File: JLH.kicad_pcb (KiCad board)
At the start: 2 copper layers, 170 x 200 mm, 51 parts, among them J1 Вход, J2 Выход, J3 B2P-VH, Q1 КТ361Г, Q2 КТ801А, Q3 2Т803А, Q4 2Т803А, Q5 КТ361Г, Q6 КТ801А, Q7 2Т803А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

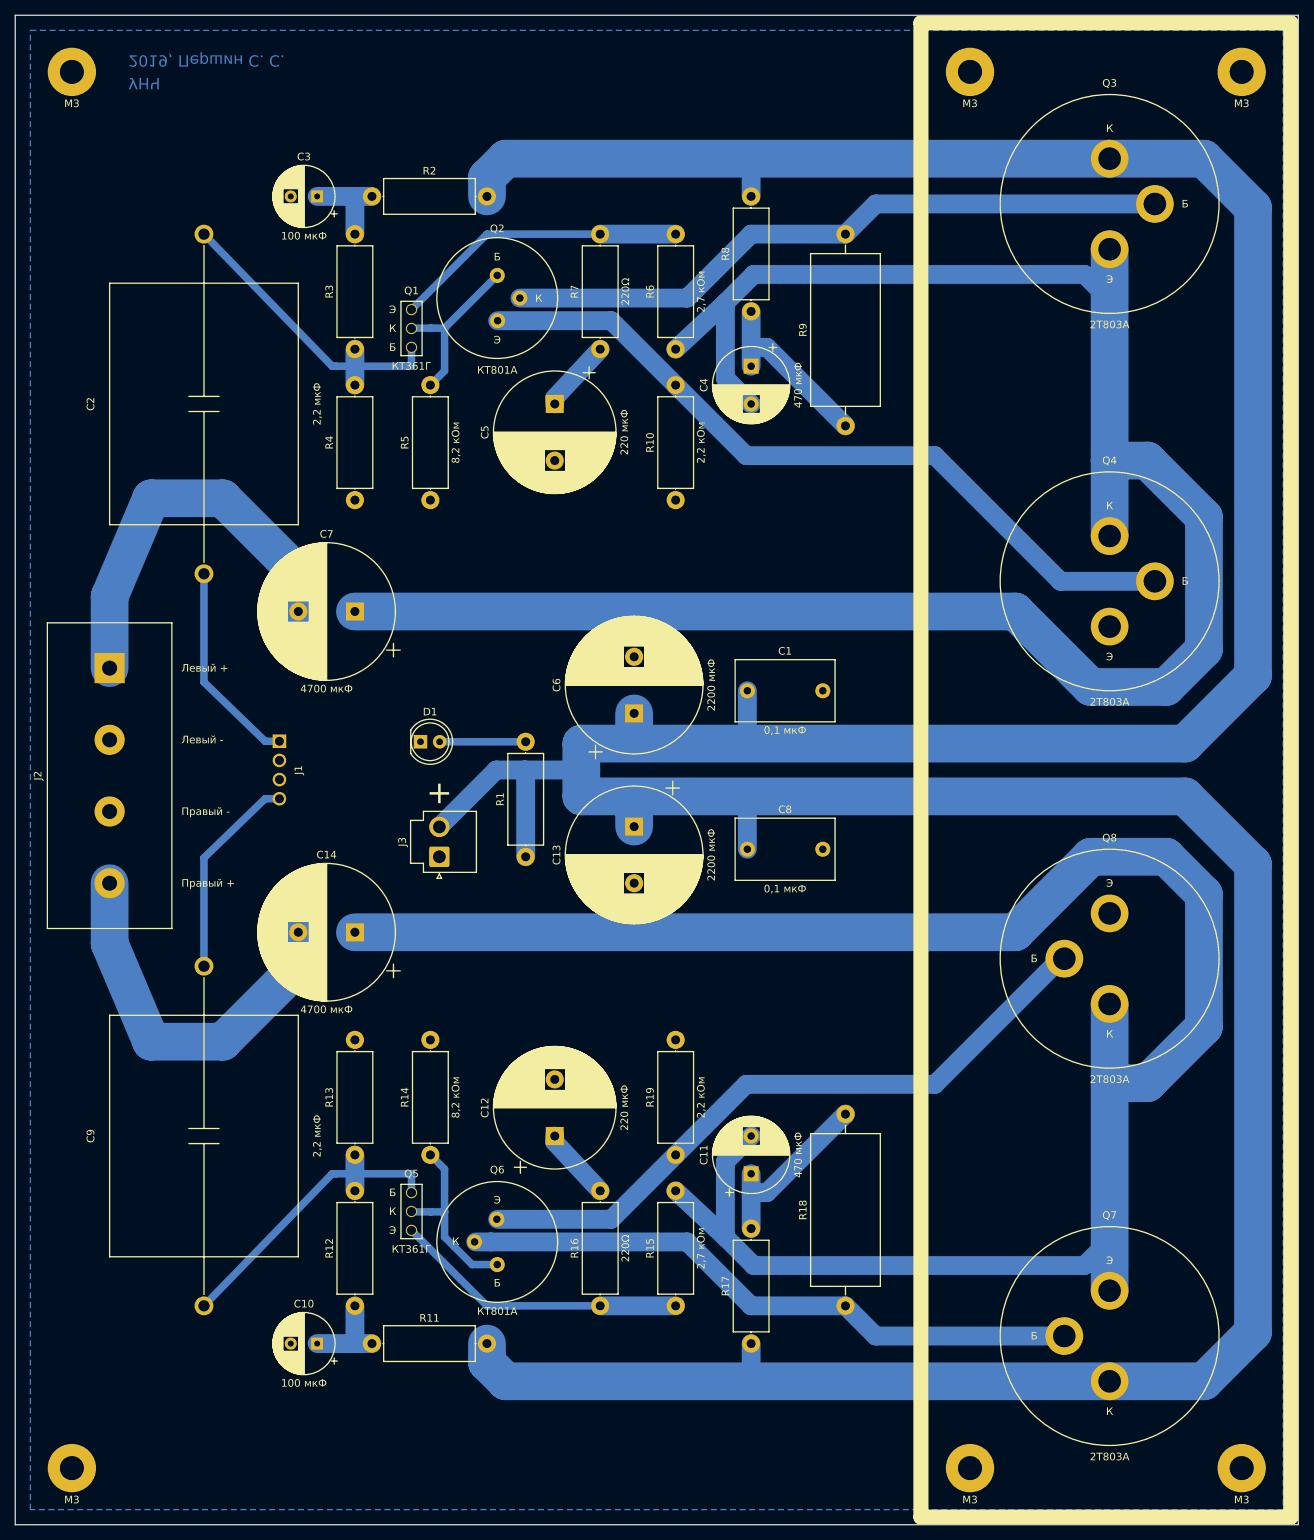
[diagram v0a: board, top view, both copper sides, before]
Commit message: Fixed GND
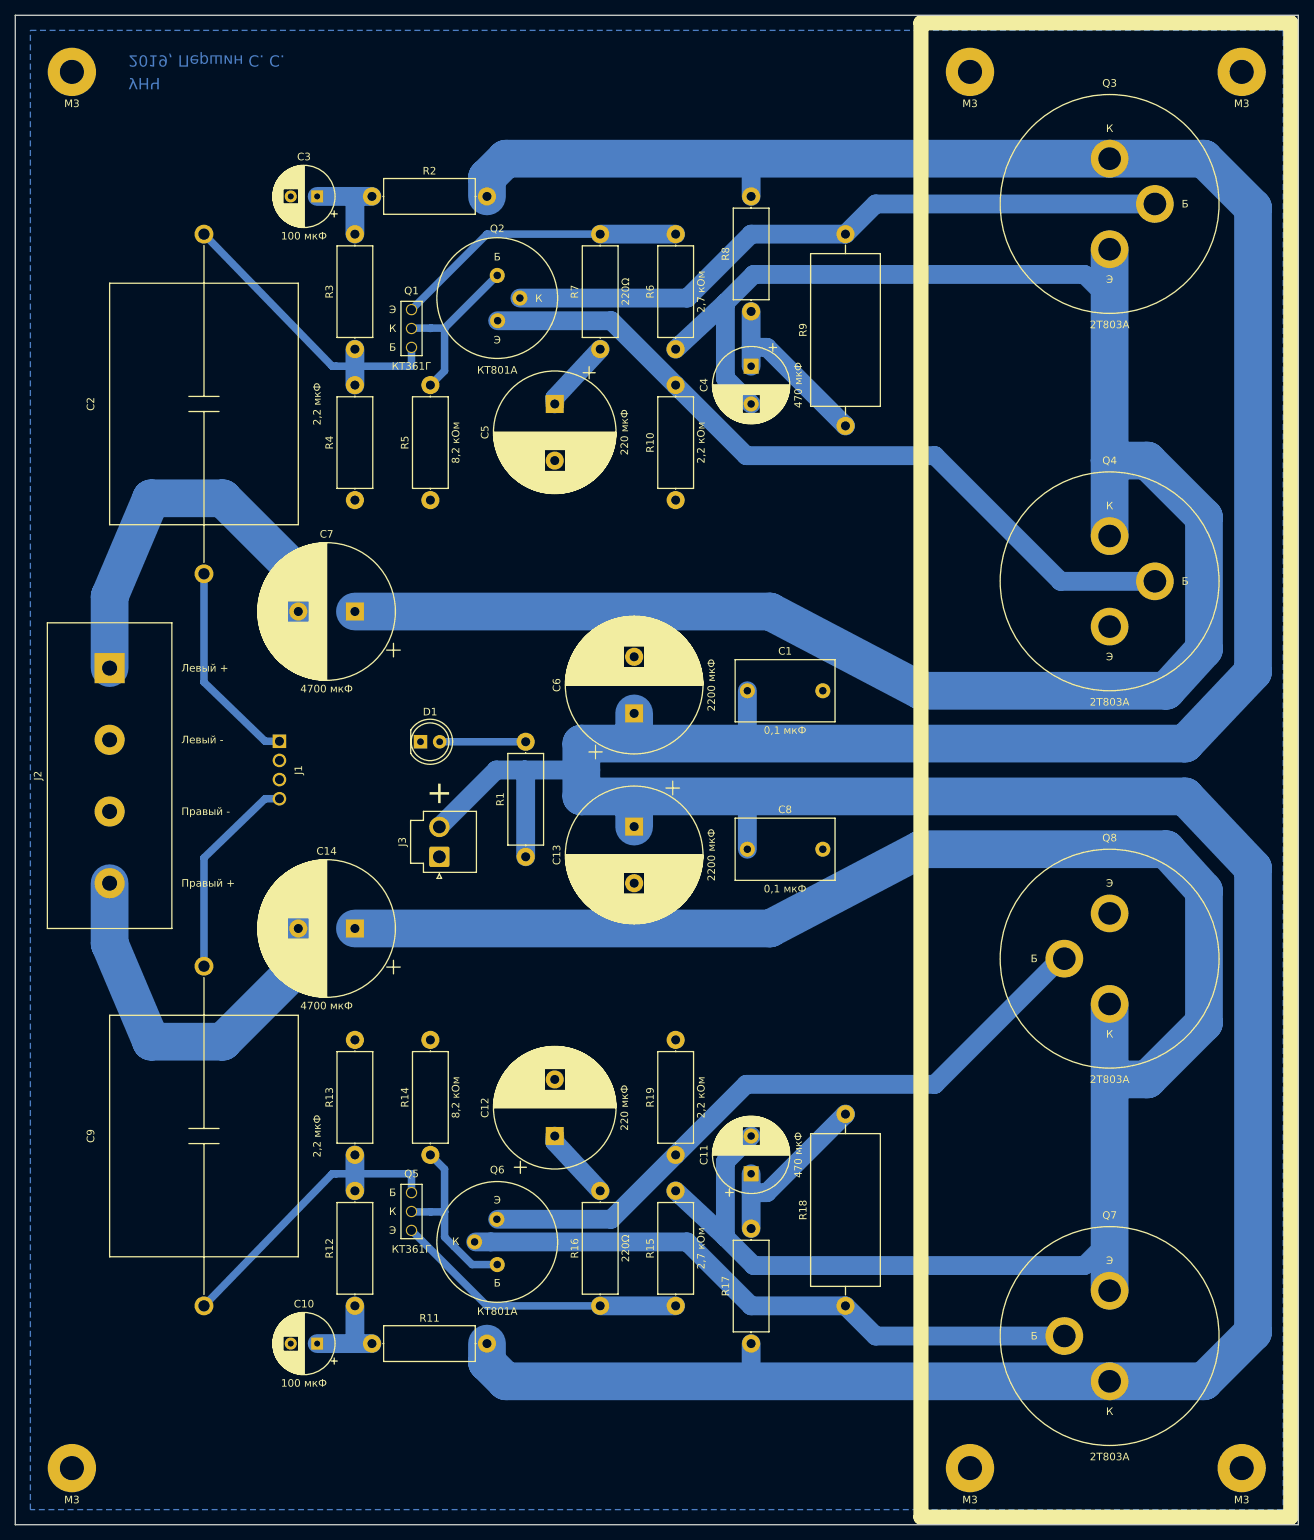
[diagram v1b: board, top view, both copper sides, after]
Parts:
- moved C14 0.50 mm to (65.0, 147.0)
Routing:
- net Net-(C4-Pad2): track 265.8 -> 264.6 mm
- net Net-(C11-Pad2): track 265.8 -> 264.6 mm
- net /Правый канал/OUT+: track 50.3 -> 50.8 mm
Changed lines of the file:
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@@
     (solder_mask_min_width 0.25)
     (aux_axis_origin 0 0)
-    (visible_elements 7FFFFFFF)
+    (visible_elements 7FFFEFFF)
     (pcbplotparams
       (layerselection 0x010fc_ffffffff)
@@
   )
   (module Capacitor_THT:CP_Radial_D18.0mm_P7.50mm (layer F.Cu)
-    (at 65 147.5 180)
+    (at 65 147 180)
     (descr "CP, Radial series, Radial, pin pitch=7.50mm, , diameter=18mm, Electrolytic Capacitor")
     (tags "CP Radial series Radial pin pitch 7.50mm  diameter 18mm Electrolytic Capacitor")
@@
   (segment (start 177.5 45) (end 165 45) (width 5) (layer B.Cu) (net 8))
   (segment (start 184 51.5) (end 177.5 45) (width 5) (layer B.Cu) (net 8))
-  (segment (start 184 113.5) (end 184 51.5) (width 5) (layer B.Cu) (net 8))
-  (segment (start 175 122.5) (end 184 113.5) (width 5) (layer B.Cu) (net 8))
+  (segment (start 184 113) (end 184 51.5) (width 5) (layer B.Cu) (net 8))
+  (segment (start 175 122.5) (end 184 113) (width 5) (layer B.Cu) (net 8))
   (segment (start 95 126) (end 95 122.5) (width 5) (layer B.Cu) (net 8))
   (segment (start 95 122.5) (end 175 122.5) (width 5) (layer B.Cu) (net 8))
@@
   (segment (start 95 129.5) (end 95 126) (width 5) (layer B.Cu) (net 8))
   (segment (start 175 129.5) (end 95 129.5) (width 5) (layer B.Cu) (net 8))
-  (segment (start 184 138.5) (end 175 129.5) (width 5) (layer B.Cu) (net 8))
-  (segment (start 184 200.5) (end 184 138.5) (width 5) (layer B.Cu) (net 8))
+  (segment (start 184 139) (end 175 129.5) (width 5) (layer B.Cu) (net 8))
+  (segment (start 184 200.5) (end 184 139) (width 5) (layer B.Cu) (net 8))
   (segment (start 177.5 207) (end 184 200.5) (width 5) (layer B.Cu) (net 8))
   (segment (start 53.1 122.19) (end 55 122.19) (width 1) (layer B.Cu) (net 9) (status 20))
@@
   (segment (start 165 57) (end 165 85) (width 5) (layer B.Cu) (net 11))
   (segment (start 165 85) (end 165 95) (width 5) (layer B.Cu) (net 11))
-  (segment (start 177.5 92.5) (end 170 85) (width 5) (layer B.Cu) (net 11))
-  (segment (start 152.5 105) (end 162.5 115) (width 5) (layer B.Cu) (net 11))
-  (segment (start 65 105) (end 152.5 105) (width 5) (layer B.Cu) (net 11))
-  (segment (start 162.5 115) (end 172.5 115) (width 5) (layer B.Cu) (net 11))
-  (segment (start 172.5 115) (end 177.5 110) (width 5) (layer B.Cu) (net 11))
-  (segment (start 170 85) (end 165 85) (width 5) (layer B.Cu) (net 11))
-  (segment (start 177.5 110) (end 177.5 92.5) (width 5) (layer B.Cu) (net 11))
+  (segment (start 120 105) (end 65 105) (width 5) (layer B.Cu) (net 11))
+  (segment (start 165 85) (end 170 85) (width 5) (layer B.Cu) (net 11))
+  (segment (start 170 85) (end 177.5 92.5) (width 5) (layer B.Cu) (net 11))
+  (segment (start 177.5 92.5) (end 177.5 110) (width 5) (layer B.Cu) (net 11))
+  (segment (start 177.5 110) (end 172.5 115.5) (width 5) (layer B.Cu) (net 11))
+  (segment (start 172.5 115.5) (end 140 115.5) (width 5) (layer B.Cu) (net 11))
+  (segment (start 140 115.5) (end 120 105) (width 5) (layer B.Cu) (net 11))
   (segment (start 91.48 76.7) (end 97.5 70.24) (width 2.5) (layer B.Cu) (net 12) (status 30))
   (segment (start 91.48 77.5) (end 91.48 76.7) (width 2.5) (layer B.Cu) (net 12) (status 30))
@@
   (segment (start 38 162) (end 32.5 149) (width 5) (layer B.Cu) (net 15))
   (segment (start 47.5 162) (end 38 162) (width 5) (layer B.Cu) (net 15))
-  (segment (start 57.5 147.5) (end 57.5 152) (width 5) (layer B.Cu) (net 15))
+  (segment (start 57.5 147) (end 57.5 152) (width 5) (layer B.Cu) (net 15))
   (segment (start 57.5 152) (end 47.5 162) (width 5) (layer B.Cu) (net 15))
   (segment (start 62.5 179.5) (end 65 179.5) (width 1) (layer B.Cu) (net 16))
@@
   (segment (start 117.5 182) (end 119.6 182) (width 2.5) (layer B.Cu) (net 18))
   (segment (start 119.6 182) (end 130 171.6) (width 2.5) (layer B.Cu) (net 18) (status 20))
+  (segment (start 172.5 136.5) (end 140 136.5) (width 5) (layer B.Cu) (net 19))
+  (segment (start 140 136.5) (end 120 147) (width 5) (layer B.Cu) (net 19))
   (segment (start 161.66 191.66) (end 163.82 189.5) (width 2.5) (layer B.Cu) (net 19))
   (segment (start 114.09 187.91) (end 117.84 191.66) (width 2.5) (layer B.Cu) (net 19))
@@
   (segment (start 107.5 181.76) (end 114.09 187.91) (width 2.5) (layer B.Cu) (net 19) (status 10))
   (segment (start 165 157) (end 165 195) (width 5) (layer B.Cu) (net 19))
-  (segment (start 152.5 147.5) (end 162.5 137.5) (width 5) (layer B.Cu) (net 19))
-  (segment (start 170 167.5) (end 165 167.5) (width 5) (layer B.Cu) (net 19))
-  (segment (start 162.5 137.5) (end 172.5 137.5) (width 5) (layer B.Cu) (net 19))
-  (segment (start 177.5 160) (end 170 167.5) (width 5) (layer B.Cu) (net 19))
-  (segment (start 65 147.5) (end 152.5 147.5) (width 5) (layer B.Cu) (net 19))
-  (segment (start 172.5 137.5) (end 177.5 142.5) (width 5) (layer B.Cu) (net 19))
-  (segment (start 177.5 142.5) (end 177.5 160) (width 5) (layer B.Cu) (net 19))
+  (segment (start 170 167) (end 165 167) (width 5) (layer B.Cu) (net 19))
+  (segment (start 177.5 159.5) (end 170 167) (width 5) (layer B.Cu) (net 19))
+  (segment (start 65 147) (end 120 147) (width 5) (layer B.Cu) (net 19))
+  (segment (start 172.5 136.5) (end 177.5 142) (width 5) (layer B.Cu) (net 19))
+  (segment (start 177.5 142) (end 177.5 159.5) (width 5) (layer B.Cu) (net 19))
   (segment (start 91.48 175.3) (end 97.5 181.76) (width 2.5) (layer B.Cu) (net 20) (status 30))
   (segment (start 91.48 174.5) (end 91.48 175.3) (width 2.5) (layer B.Cu) (net 20) (status 30))

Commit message: Added mounting hole
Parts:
- added H7: M3, MountingHole:MountingHole_3.2mm_M3_Pad, F.Cu at (182.5, 126.0)
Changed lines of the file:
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@@
     (tracks 153)
     (zones 0)
-    (modules 51)
+    (modules 52)
     (nets 26)
   )
@@
     )
   )
+  (module MountingHole:MountingHole_3.2mm_M3_Pad (layer F.Cu)
+    (at 182.5 126)
+    (descr "Mounting Hole 3.2mm, M3")
+    (tags "mounting hole 3.2mm m3")
+    (attr virtual)
+    (fp_text reference H7 (at 0 -4.2) (layer F.SilkS) hide
+      (effects (font (size 1 1) (thickness 0.15)))
+    )
+    (fp_text value M3 (at 0 4.2) (layer F.SilkS)
+      (effects (font (size 1 1) (thickness 0.15)))
+    )
+    (fp_text user %R (at 0.3 0) (layer F.Fab)
+      (effects (font (size 1 1) (thickness 0.15)))
+    )
+    (fp_circle (center 0 0) (end 3.2 0) (layer Cmts.User) (width 0.15))
+    (fp_circle (center 0 0) (end 3.45 0) (layer F.CrtYd) (width 0.05))
+    (pad 1 thru_hole circle (at 0 0) (size 6.4 6.4) (drill 3.2) (layers *.Cu *.Mask))
+  )
   (gr_text "2019, Першин С. С." (at 35 32 -180) (layer B.Cu)

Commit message: Updated PCB
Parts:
- moved J3 11.6 mm to (75.0, 126.0), turned to 0 degrees
- moved D1 9.85 mm to (75.0, 112.5)
- moved R1 7.50 mm to (87.5, 130.0)
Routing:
- net /Левый канал/VCC: track 582.1 -> 568.7 mm
- net Net-(D1-Pad2): track 11.4 -> 10.9 mm
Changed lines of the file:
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@@
   )
   (setup
-    (last_trace_width 0.25)
+    (last_trace_width 2.5)
     (user_trace_width 1)
     (user_trace_width 2.5)
@@
   )
   (module LED_THT:LED_D5.0mm (layer F.Cu)
-    (at 73.69 122.26)
+    (at 75 112.5)
     (descr "LED, diameter 5.0mm, 2 pins, http://cdn-reichelt.de/documents/datenblatt/A500/LL-504BC2E-009.pdf")
     (tags "LED diameter 5.0mm 2 pins")
@@
   (module JLH:5-103639-3 (layer F.Cu)
     (at 55 122.19 270)
-    (fp_text reference J1 (at 3.81 -2.54 270) (layer F.SilkS)
+    (fp_text reference J1 (at 3.81 4 270) (layer F.SilkS)
       (effects (font (size 1 1) (thickness 0.15)))
     )
-    (fp_text value Вход (at 3.81 2.54 270) (layer F.Fab)
+    (fp_text value Вход (at 3.81 -4 270) (layer F.SilkS)
       (effects (font (size 1 1) (thickness 0.15)))
     )
@@
       (effects (font (size 1 1) (thickness 0.15)))
     )
-    (fp_text value Выход (at 14.25 -9.5 270) (layer F.Fab)
+    (fp_text value Выход (at 14.25 -9.5 270) (layer F.SilkS)
       (effects (font (size 1 1) (thickness 0.15)))
     )
@@
   )
   (module Connector_JST:JST_VH_B2P-VH_1x02_P3.96mm_Vertical (layer F.Cu)
-    (at 76.19 137.5 90)
+    (at 75 126)
     (descr "JST VH series connector, B2P-VH (http://www.jst-mfg.com/product/pdf/eng/eVH.pdf), generated with kicad-footprint-generator")
     (tags "connector JST VH side entry")
-    (fp_text reference J3 (at 1.98 -4.9 270) (layer F.SilkS)
+    (fp_text reference J3 (at 1.98 -4.9 180) (layer F.SilkS)
       (effects (font (size 1 1) (thickness 0.15)))
     )
-    (fp_text value B2P-VH (at 1.98 6 270) (layer F.Fab)
+    (fp_text value B2P-VH (at 1.98 6 180) (layer F.Fab)
       (effects (font (size 1 1) (thickness 0.15)))
     )
@@
     (fp_line (start -2.86 0.3) (end -2.86 -0.3) (layer F.SilkS) (width 0.12))
     (fp_line (start -2.86 -0.3) (end -2.26 0) (layer F.SilkS) (width 0.12))
-    (fp_text user %R (at 1.98 4.1 270) (layer F.Fab)
+    (fp_text user %R (at 1.98 4.1 180) (layer F.Fab)
       (effects (font (size 1 1) (thickness 0.15)))
     )
-    (pad 1 thru_hole roundrect (at 0 0 90) (size 2.7 2.7) (drill 1.7) (layers *.Cu *.Mask) (roundrect_rratio 0.09259299999999999)
+    (pad 1 thru_hole roundrect (at 0 0) (size 2.7 2.7) (drill 1.7) (layers *.Cu *.Mask) (roundrect_rratio 0.09259299999999999)
       (net 4 GND))
-    (pad 2 thru_hole circle (at 3.96 0 90) (size 2.7 2.7) (drill 1.7) (layers *.Cu *.Mask)
+    (pad 2 thru_hole circle (at 3.96 0) (size 2.7 2.7) (drill 1.7) (layers *.Cu *.Mask)
       (net 8 "/Левый канал/VCC"))
     (model ${KISYS3DMOD}/Connector_JST.3dshapes/JST_VH_B2P-VH_1x02_P3.96mm_Vertical.wrl
@@
   )
   (module Resistor_THT:R_Axial_DIN0414_L11.9mm_D4.5mm_P15.24mm_Horizontal (layer F.Cu)
-    (at 87.63 137.5 90)
+    (at 87.5 130 90)
     (descr "Resistor, Axial_DIN0414 series, Axial, Horizontal, pin pitch=15.24mm, 2W, length*diameter=11.9*4.5mm^2, http://www.vishay.com/docs/20128/wkxwrx.pdf")
     (tags "Resistor Axial_DIN0414 series Axial Horizontal pin pitch 15.24mm 2W length 11.9mm diameter 4.5mm")
@@
   (gr_line (start 190 26) (end 190 226) (layer Edge.Cuts) (width 0.05))
   (gr_line (start 190 26) (end 20 26) (layer Edge.Cuts) (width 0.05))
-  (gr_text + (at 76.19 129) (layer F.SilkS)
+  (gr_text + (at 78.96 133) (layer F.SilkS)
     (effects (font (size 3 3) (thickness 0.15)))
   )
@@
   (segment (start 82.5 202) (end 82.5 204.5) (width 5) (layer B.Cu) (net 8))
   (segment (start 82.5 204.5) (end 85 207) (width 5) (layer B.Cu) (net 8))
-  (segment (start 83.73 126) (end 76.19 133.54) (width 2.5) (layer B.Cu) (net 8))
-  (segment (start 87.63 126.13) (end 87.5 126) (width 2.5) (layer B.Cu) (net 8))
-  (segment (start 87.63 137.5) (end 87.63 126.13) (width 2.5) (layer B.Cu) (net 8))
-  (segment (start 95 126) (end 87.5 126) (width 2.5) (layer B.Cu) (net 8))
-  (segment (start 87.5 126) (end 83.73 126) (width 2.5) (layer B.Cu) (net 8))
   (segment (start 102 118.5) (end 102 120) (width 5) (layer B.Cu) (net 8))
   (segment (start 102 133.5) (end 102 132) (width 5) (layer B.Cu) (net 8))
@@
   (segment (start 184 200.5) (end 184 139) (width 5) (layer B.Cu) (net 8))
   (segment (start 177.5 207) (end 184 200.5) (width 5) (layer B.Cu) (net 8))
+  (segment (start 95 126) (end 87.5 126) (width 5) (layer B.Cu) (net 8))
+  (segment (start 87.5 126) (end 82.5 126) (width 5) (layer B.Cu) (net 8))
+  (segment (start 78.96 126) (end 82.5 126) (width 2.5) (layer B.Cu) (net 8))
+  (segment (start 87.5 130) (end 87.5 126) (width 2.5) (layer B.Cu) (net 8))
   (segment (start 53.1 122.19) (end 55 122.19) (width 1) (layer B.Cu) (net 9) (status 20))
   (segment (start 45 114.36) (end 53.1 122.19) (width 1) (layer B.Cu) (net 9))
@@
   (segment (start 91.48 175.3) (end 97.5 181.76) (width 2.5) (layer B.Cu) (net 20) (status 30))
   (segment (start 91.48 174.5) (end 91.48 175.3) (width 2.5) (layer B.Cu) (net 20) (status 30))
-  (segment (start 87.63 122.26) (end 76.23 122.26) (width 1) (layer B.Cu) (net 21))
+  (segment (start 85.24 112.5) (end 87.5 114.76) (width 2.5) (layer B.Cu) (net 21))
+  (segment (start 77.54 112.5) (end 85.24 112.5) (width 2.5) (layer B.Cu) (net 21))
   (segment (start 107.5 197) (end 97.5 197) (width 2.5) (layer B.Cu) (net 22))
   (segment (start 72.5 187) (end 82.5 197) (width 1) (layer B.Cu) (net 22))
